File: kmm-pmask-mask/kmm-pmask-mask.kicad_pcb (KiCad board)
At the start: 4 copper layers, 90.4 x 109 mm, 39 parts, among them J1 F31L-1A7H1-11030, U1 MS5611-01BA, U10 MAX30101EFD_T, U11 SHT40-AD1B-R3, U12 SHT40-AD1B-R3, U13 TMP117MAIDRVR, U14 TMP117MAIDRVR, U15 TCA9546APW, U2 MAX30101EFD_T, U3 SHT40-AD1B-R3, U4 TMP117MAIDRVR, U5 MS5611-01BA, U6 MS5611-01BA, U7 MS5611-01BA, U8 MAX30101EFD_T, U9 MAX30101EFD_T

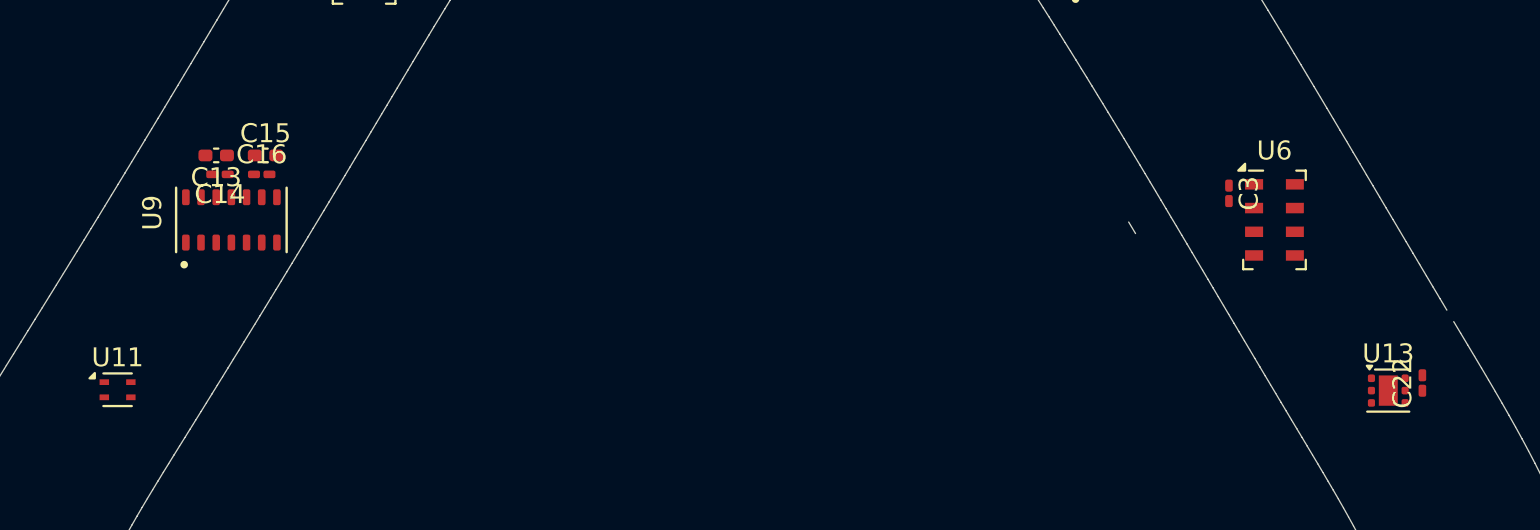
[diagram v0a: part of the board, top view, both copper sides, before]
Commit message: tweak positions, move components away from edge
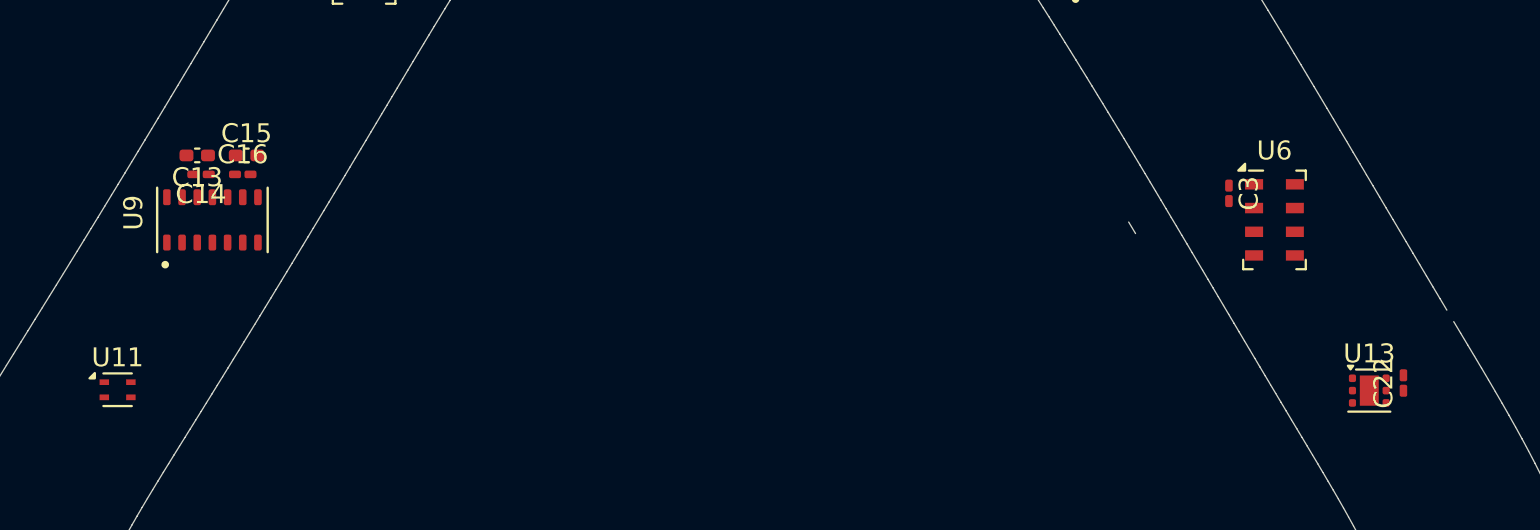
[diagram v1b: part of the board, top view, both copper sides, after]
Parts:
- moved C13 1.00 mm to (46.2, 96.6)
- moved C14 1.00 mm to (46.4, 97.6)
- moved C15 1.00 mm to (48.8, 96.6)
- moved C16 1.00 mm to (48.6, 97.6)
- moved C22 1.00 mm to (109.8, 108.6)
- moved U13 1.00 mm to (108.0, 109.0)
- moved U9 1.00 mm to (47.0, 100.0)
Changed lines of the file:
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@@
 	(footprint "kmm-pmask:MAX30101EFD_T"
 		(layer "F.Cu")
-		(at 48 100 90)
+		(at 47 100 90)
 		(property "Reference" "U9"
 			(at 0.37746 -4.16481 90)
@@
 	(footprint "Capacitor_SMD:C_0201_0603Metric_Pad0.64x0.40mm_HandSolder"
 		(layer "F.Cu")
-		(at 47.4 97.6 180)
+		(at 46.4 97.6 180)
 		(descr "Capacitor SMD 0201 (0603 Metric), square (rectangular) end terminal, IPC-7351 nominal with elongated pad for handsoldering. (Body size source: https://www.vishay.com/docs/20052/crcw0201e3.pdf)")
 		(tags "capacitor handsolder")
@@
 	(footprint "Capacitor_SMD:C_0201_0603Metric_Pad0.64x0.40mm_HandSolder"
 		(layer "F.Cu")
-		(at 110.8 108.6 90)
+		(at 109.8 108.6 90)
 		(descr "Capacitor SMD 0201 (0603 Metric), square (rectangular) end terminal, IPC-7351 nominal with elongated pad for handsoldering. (Body size source: https://www.vishay.com/docs/20052/crcw0201e3.pdf)")
 		(tags "capacitor handsolder")
@@
 	(footprint "Package_SON:WSON-6-1EP_2x2mm_P0.65mm_EP1x1.6mm"
 		(layer "F.Cu")
-		(at 109 109)
+		(at 108 109)
 		(descr "WSON, 6 Pin (http://www.ti.com/lit/ds/symlink/tps61040.pdf#page=35)")
 		(tags "WSON NoLead")
@@
 	(footprint "Capacitor_SMD:C_0402_1005Metric_Pad0.74x0.62mm_HandSolder"
 		(layer "F.Cu")
-		(at 47.2 96.6 180)
+		(at 46.2 96.6 180)
 		(descr "Capacitor SMD 0402 (1005 Metric), square (rectangular) end terminal, IPC-7351 nominal with elongated pad for handsoldering. (Body size source: IPC-SM-782 page 76, https://www.pcb-3d.com/wordpress/wp-content/uploads/ipc-sm-782a_amendment_1_and_2.pdf)")
 		(tags "capacitor handsolder")
@@
 	(footprint "Capacitor_SMD:C_0402_1005Metric_Pad0.74x0.62mm_HandSolder"
 		(layer "F.Cu")
-		(at 49.8 96.6)
+		(at 48.8 96.6)
 		(descr "Capacitor SMD 0402 (1005 Metric), square (rectangular) end terminal, IPC-7351 nominal with elongated pad for handsoldering. (Body size source: IPC-SM-782 page 76, https://www.pcb-3d.com/wordpress/wp-content/uploads/ipc-sm-782a_amendment_1_and_2.pdf)")
 		(tags "capacitor handsolder")
@@
 	(footprint "Capacitor_SMD:C_0201_0603Metric_Pad0.64x0.40mm_HandSolder"
 		(layer "F.Cu")
-		(at 49.6 97.6)
+		(at 48.6 97.6)
 		(descr "Capacitor SMD 0201 (0603 Metric), square (rectangular) end terminal, IPC-7351 nominal with elongated pad for handsoldering. (Body size source: https://www.vishay.com/docs/20052/crcw0201e3.pdf)")
 		(tags "capacitor handsolder")
@@
 	)
 	(gr_line
-		(start 48 30)
-		(end 48 160)
+		(start 47 30)
+		(end 47 160)
 		(stroke
 			(width 0.1)
@@
 	)
 	(gr_line
-		(start 109 30)
-		(end 109 160)
+		(start 108 30)
+		(end 108 160)
 		(stroke
 			(width 0.1)
@@
 		(layer "Dwgs.User")
 		(pts
-			(xy 109 160) (xy 103 160)
+			(xy 47 160) (xy 42 160)
 		)
 		(height 0)
@@
 			(keep_text_aligned yes)
 		)
-		(gr_text "6"
-			(at 106 158.85 0)
+		(gr_text "5"
+			(at 44.5 158.85 0)
 			(layer "Dwgs.User")
 			(effects
@@
 		(layer "Dwgs.User")
 		(pts
-			(xy 48 160) (xy 42 160)
+			(xy 108 160) (xy 103 160)
 		)
 		(height 0)
@@
 			(keep_text_aligned yes)
 		)
-		(gr_text "6"
-			(at 45 158.85 0)
+		(gr_text "5"
+			(at 105.5 158.85 0)
 			(layer "Dwgs.User")
 			(effects
@@
 		(layer "Dwgs.User")
 		(pts
-			(xy 55 160) (xy 48 160)
+			(xy 125 100) (xy 125 109)
 		)
 		(height 0)
-		(orientation 0)
+		(orientation 1)
 		(format
 			(prefix "")
@@
 			(keep_text_aligned yes)
 		)
-		(gr_text "7"
-			(at 51.5 158.85 0)
+		(gr_text "9"
+			(at 123.85 104.5 90)
 			(layer "Dwgs.User")
 			(effects
@@
 		(layer "Dwgs.User")
 		(pts
-			(xy 125 100) (xy 125 109)
+			(xy 130 150) (xy 130 160)
 		)
 		(height 0)
@@
 			(keep_text_aligned yes)
 		)
-		(gr_text "9"
-			(at 123.85 104.5 90)
+		(gr_text "10"
+			(at 128.85 155 90)
 			(layer "Dwgs.User")
 			(effects
@@
 		(layer "Dwgs.User")
 		(pts
-			(xy 130 150) (xy 130 160)
+			(xy 125 109) (xy 125 143)
 		)
 		(height 0)
@@
 			(keep_text_aligned yes)
 		)
-		(gr_text "10"
-			(at 128.85 155 90)
+		(gr_text "34"
+			(at 123.85 126 90)
 			(layer "Dwgs.User")
 			(effects
@@
 		(layer "Dwgs.User")
 		(pts
-			(xy 125 109) (xy 125 143)
+			(xy 140 150) (xy 130 150)
 		)
 		(height 0)
-		(orientation 1)
+		(orientation 0)
 		(format
 			(prefix "")
@@
 			(keep_text_aligned yes)
 		)
-		(gr_text "34"
-			(at 123.85 126 90)
+		(gr_text "10"
+			(at 135 148.85 0)
 			(layer "Dwgs.User")
 			(effects
@@
 		(layer "Dwgs.User")
 		(pts
-			(xy 140 150) (xy 130 150)
+			(xy 55 160) (xy 47 160)
 		)
 		(height 0)
@@
 			(keep_text_aligned yes)
 		)
-		(gr_text "10"
-			(at 135 148.85 0)
+		(gr_text "8"
+			(at 51 158.85 0)
 			(layer "Dwgs.User")
 			(effects

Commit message: Mostly annotate schematic
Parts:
- added C24: 100n, Capacitor_SMD:C_0201_0603Metric_Pad0.64x0.40mm_HandSolder, F.Cu at (157.9, 87.4)
- added C25: 100n, Capacitor_SMD:C_0201_0603Metric_Pad0.64x0.40mm_HandSolder, F.Cu at (157.9, 89.1)
- added C26: 100n, Capacitor_SMD:C_0201_0603Metric_Pad0.64x0.40mm_HandSolder, F.Cu at (157.9, 90.9)
- added R1: 4.7k, Resistor_SMD:R_0201_0603Metric_Pad0.64x0.40mm_HandSolder, F.Cu at (157.9, 92.6)
- added R2: 4.7k, Resistor_SMD:R_0201_0603Metric_Pad0.64x0.40mm_HandSolder, F.Cu at (157.9, 94.4)
- added R3: 4.7k, Resistor_SMD:R_0201_0603Metric_Pad0.64x0.40mm_HandSolder, F.Cu at (157.9, 96.1)
- added R4: 4.7k, Resistor_SMD:R_0201_0603Metric_Pad0.64x0.40mm_HandSolder, F.Cu at (160.7, 87.4)
- added R5: 4.7k, Resistor_SMD:R_0201_0603Metric_Pad0.64x0.40mm_HandSolder, F.Cu at (160.7, 89.1)
- added R6: 4.7k, Resistor_SMD:R_0201_0603Metric_Pad0.64x0.40mm_HandSolder, F.Cu at (160.7, 90.9)
- added R7: 4.7k, Resistor_SMD:R_0201_0603Metric_Pad0.64x0.40mm_HandSolder, F.Cu at (160.7, 92.6)
- added R8: 4.7k, Resistor_SMD:R_0201_0603Metric_Pad0.64x0.40mm_HandSolder, F.Cu at (160.7, 94.4)
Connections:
- net +1V8 renamed +1.8V
- U1 pad 7: unconnected-(U1-SDI/SDA-Pad7) -> /I2C0_SDA
- U1 pad 8: unconnected-(U1-SCLK-Pad8) -> /I2C0_SCL
- U10 pad 2: unconnected-(U10-SCL-Pad2) -> /I2C3_SCL
- U10 pad 3: unconnected-(U10-SDA-Pad3) -> /I2C3_SDA
- U11 pad 1: unconnected-(U11-SDA-Pad1) -> /I2C1_SDA
- U11 pad 2: unconnected-(U11-SCL-Pad2) -> /I2C1_SCL
- U12 pad 1: unconnected-(U12-SDA-Pad1) -> /I2C1_SDA
- U12 pad 2: unconnected-(U12-SCL-Pad2) -> /I2C1_SCL
- U13 pad 1: unconnected-(U13-SCL-Pad1) -> /I2C2_SCL
- U13 pad 4: +3.3V -> GND
- U13 pad 6: unconnected-(U13-SDA-Pad6) -> /I2C2_SDA
- U14 pad 1: unconnected-(U14-SCL-Pad1) -> /I2C3_SCL
- U14 pad 6: unconnected-(U14-SDA-Pad6) -> /I2C3_SDA
- U15 pad 10: unconnected-(U15-SC2-Pad10) -> /I2C2_SCL
- U15 pad 11: unconnected-(U15-SD3-Pad11) -> /I2C3_SDA
- U15 pad 12: unconnected-(U15-SC3-Pad12) -> /I2C3_SCL
- U15 pad 14: unconnected-(U15-SCL-Pad14) -> /I2C_M_SCL
- U15 pad 15: unconnected-(U15-SDA-Pad15) -> /I2C_M_SDA
- U15 pad 3: unconnected-(U15-~{RESET}-Pad3) -> /~{I2C_M_RST}
- U15 pad 4: unconnected-(U15-SD0-Pad4) -> /I2C0_SDA
- U15 pad 5: unconnected-(U15-SC0-Pad5) -> /I2C0_SCL
- U15 pad 6: unconnected-(U15-SD1-Pad6) -> /I2C1_SDA
- U15 pad 7: unconnected-(U15-SC1-Pad7) -> /I2C1_SCL
- U15 pad 9: unconnected-(U15-SD2-Pad9) -> /I2C2_SDA
- U2 pad 2: unconnected-(U2-SCL-Pad2) -> /I2C0_SCL
- U2 pad 3: unconnected-(U2-SDA-Pad3) -> /I2C0_SDA
- U3 pad 1: unconnected-(U3-SDA-Pad1) -> /I2C1_SDA
- U3 pad 2: unconnected-(U3-SCL-Pad2) -> /I2C1_SCL
- U4 pad 1: unconnected-(U4-SCL-Pad1) -> /I2C1_SCL
- U4 pad 4: Net-(U4-ADD0) -> GND
- U4 pad 6: Net-(U4-ADD0) -> /I2C1_SDA
- U5 pad 7: unconnected-(U5-SDI/SDA-Pad7) -> /I2C1_SDA
- U5 pad 8: unconnected-(U5-SCLK-Pad8) -> /I2C1_SCL
- U6 pad 7: unconnected-(U6-SDI/SDA-Pad7) -> /I2C2_SDA
- U6 pad 8: unconnected-(U6-SCLK-Pad8) -> /I2C2_SCL
- U7 pad 7: unconnected-(U7-SDI/SDA-Pad7) -> /I2C3_SDA
- U7 pad 8: unconnected-(U7-SCLK-Pad8) -> /I2C3_SCL
- U8 pad 2: unconnected-(U8-SCL-Pad2) -> /I2C2_SCL
- U8 pad 3: unconnected-(U8-SDA-Pad3) -> /I2C2_SDA
- U9 pad 2: unconnected-(U9-SCL-Pad2) -> /I2C1_SCL
- U9 pad 3: unconnected-(U9-SDA-Pad3) -> /I2C1_SDA
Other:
- outline, holes or cut-outs redrawn

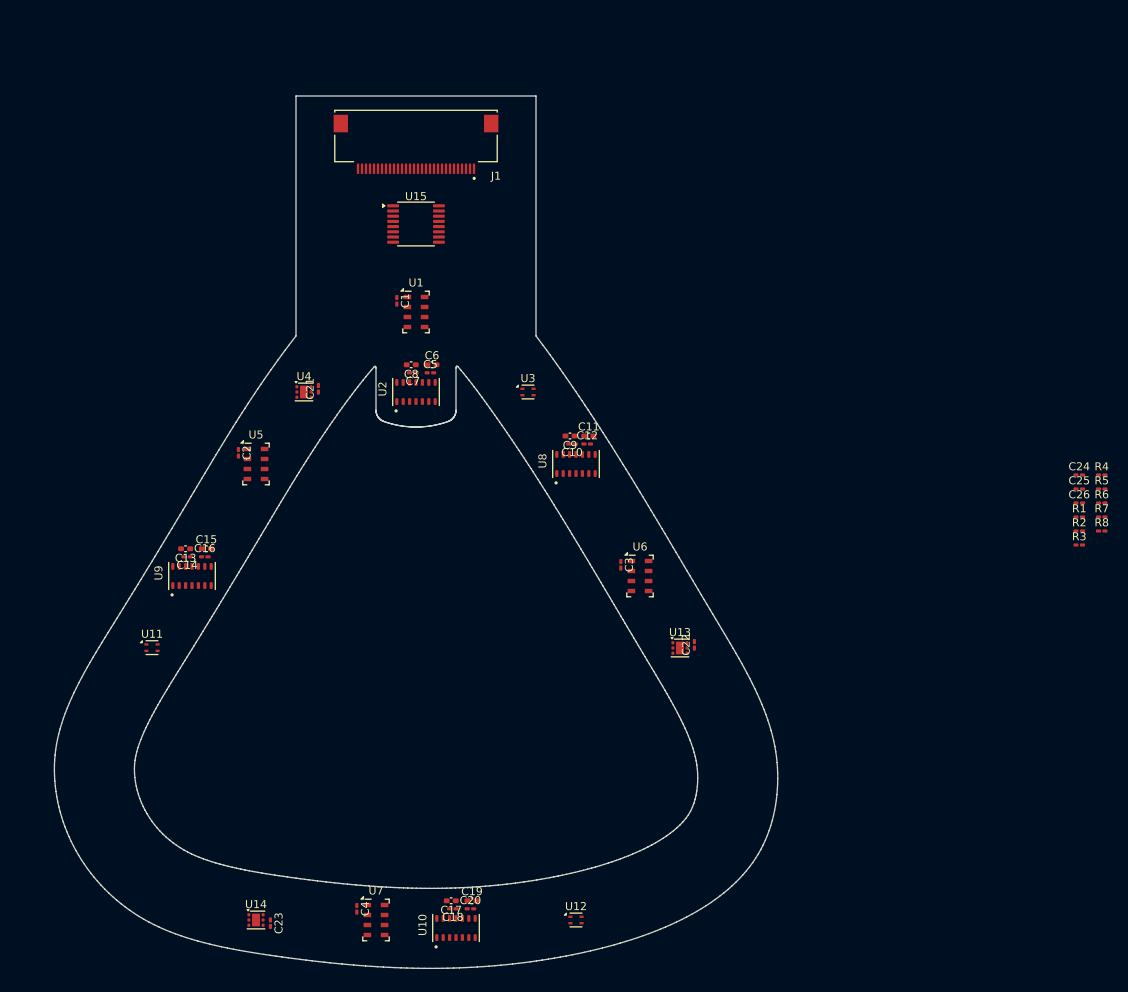
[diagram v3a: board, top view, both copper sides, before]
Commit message: add extra decoupling caps, pull-ups to placement
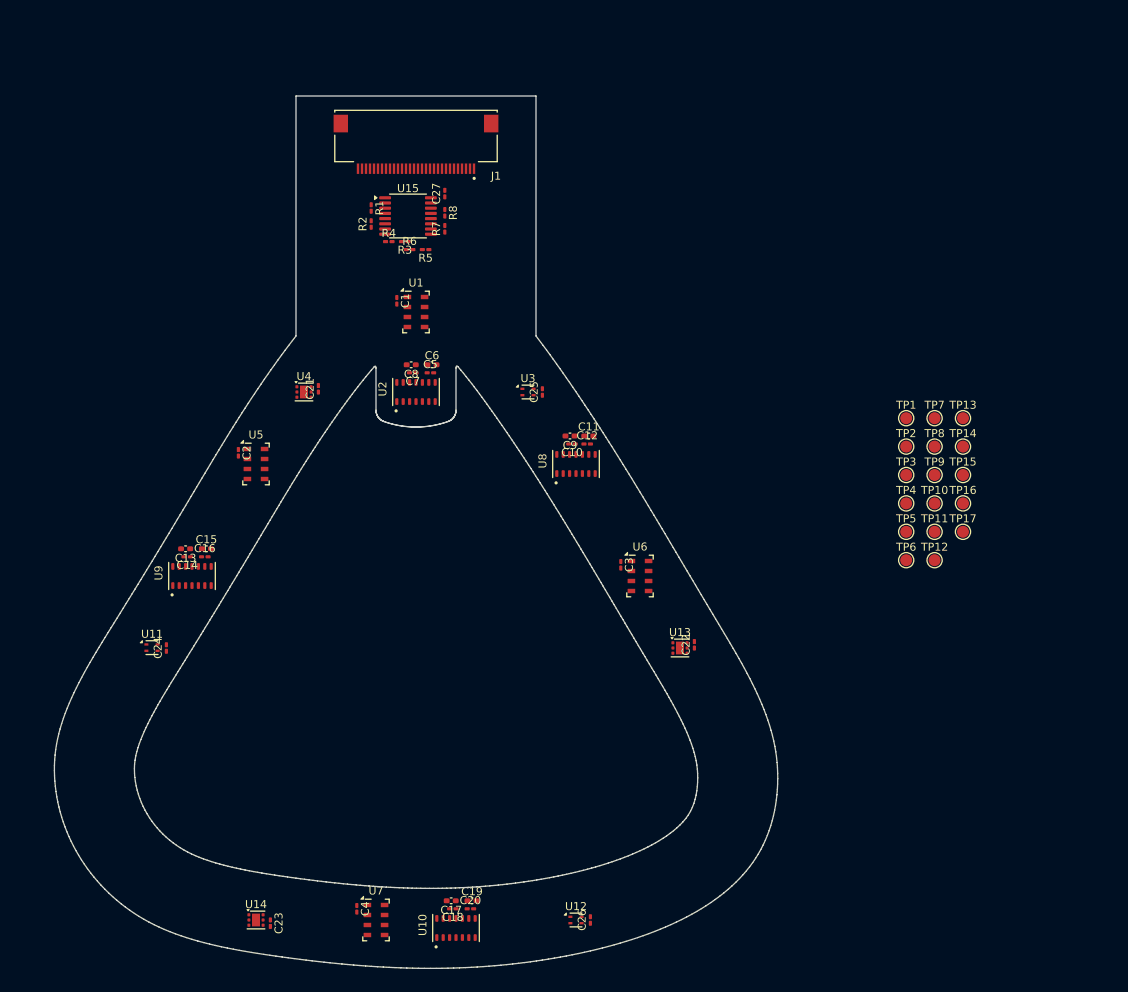
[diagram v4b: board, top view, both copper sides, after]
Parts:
- added C27: 100n, Capacitor_SMD:C_0201_0603Metric_Pad0.64x0.40mm_HandSolder, F.Cu at (78.6, 52.2)
- added TP1: I2C0 SDA, TestPoint:TestPoint_Pad_D1.5mm, F.Cu at (136.3, 80.3)
- added TP10: I2C M SCL, TestPoint:TestPoint_Pad_D1.5mm, F.Cu at (139.8, 90.9)
- added TP11: 5V, TestPoint:TestPoint_Pad_D1.5mm, F.Cu at (139.8, 94.5)
- added TP12: 3.3V, TestPoint:TestPoint_Pad_D1.5mm, F.Cu at (139.8, 98.0)
- added TP13: 1.8V, TestPoint:TestPoint_Pad_D1.5mm, F.Cu at (143.4, 80.3)
- added TP14: GND, TestPoint:TestPoint_Pad_D1.5mm, F.Cu at (143.4, 83.8)
- added TP15: GND, TestPoint:TestPoint_Pad_D1.5mm, F.Cu at (143.4, 87.4)
- added TP16: GND, TestPoint:TestPoint_Pad_D1.5mm, F.Cu at (143.4, 90.9)
- added TP17: GND, TestPoint:TestPoint_Pad_D1.5mm, F.Cu at (143.4, 94.5)
- added TP2: I2C0 SCL, TestPoint:TestPoint_Pad_D1.5mm, F.Cu at (136.3, 83.8)
- added TP3: I2C1 SDA, TestPoint:TestPoint_Pad_D1.5mm, F.Cu at (136.3, 87.4)
- added TP4: I2C1 SCL, TestPoint:TestPoint_Pad_D1.5mm, F.Cu at (136.3, 90.9)
- added TP5: I2C2 SDA, TestPoint:TestPoint_Pad_D1.5mm, F.Cu at (136.3, 94.5)
- added TP6: I2C2 SCL, TestPoint:TestPoint_Pad_D1.5mm, F.Cu at (136.3, 98.0)
- added TP7: I2C3 SDA, TestPoint:TestPoint_Pad_D1.5mm, F.Cu at (139.8, 80.3)
- added TP8: I2C3 SCL, TestPoint:TestPoint_Pad_D1.5mm, F.Cu at (139.8, 83.8)
- added TP9: I2C M SDA, TestPoint:TestPoint_Pad_D1.5mm, F.Cu at (139.8, 87.4)
- moved C24 116.1 mm to (43.8, 109.0), turned to 90 degrees
- moved R1 96.6 mm to (69.4, 54.0), turned to -90 degrees
- moved R2 96.5 mm to (69.4, 56.0), turned to 90 degrees
- moved R4 93.8 mm to (71.6, 58.2)
- moved R3 92.4 mm to (73.6, 58.2), turned to 180 degrees
- moved R6 92.1 mm to (74.2, 59.2)
- moved R8 91.2 mm to (78.6, 54.6), turned to -90 degrees
- moved R7 89.7 mm to (78.6, 56.6), turned to 90 degrees
- moved R5 89.7 mm to (76.2, 59.2), turned to 180 degrees
- moved C26 80.3 mm to (96.8, 143.0), turned to 90 degrees
- moved C25 68.2 mm to (90.8, 77.0), turned to 90 degrees
- moved U15 1.41 mm to (74.0, 55.0)
